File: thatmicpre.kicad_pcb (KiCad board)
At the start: 2 copper layers, 119.1 x 74.2 mm, 79 parts, among them J1 Barrel_Jack_Switch, J2 NC3FBH1, J3 NC3MBH2, Q1 BC546B, Q2 BC546B, SW1 SW_DPDT_x2, SW2 SW_DPDT_x2, SW3 SW_Rotary12, U1 THAT1510P08-U

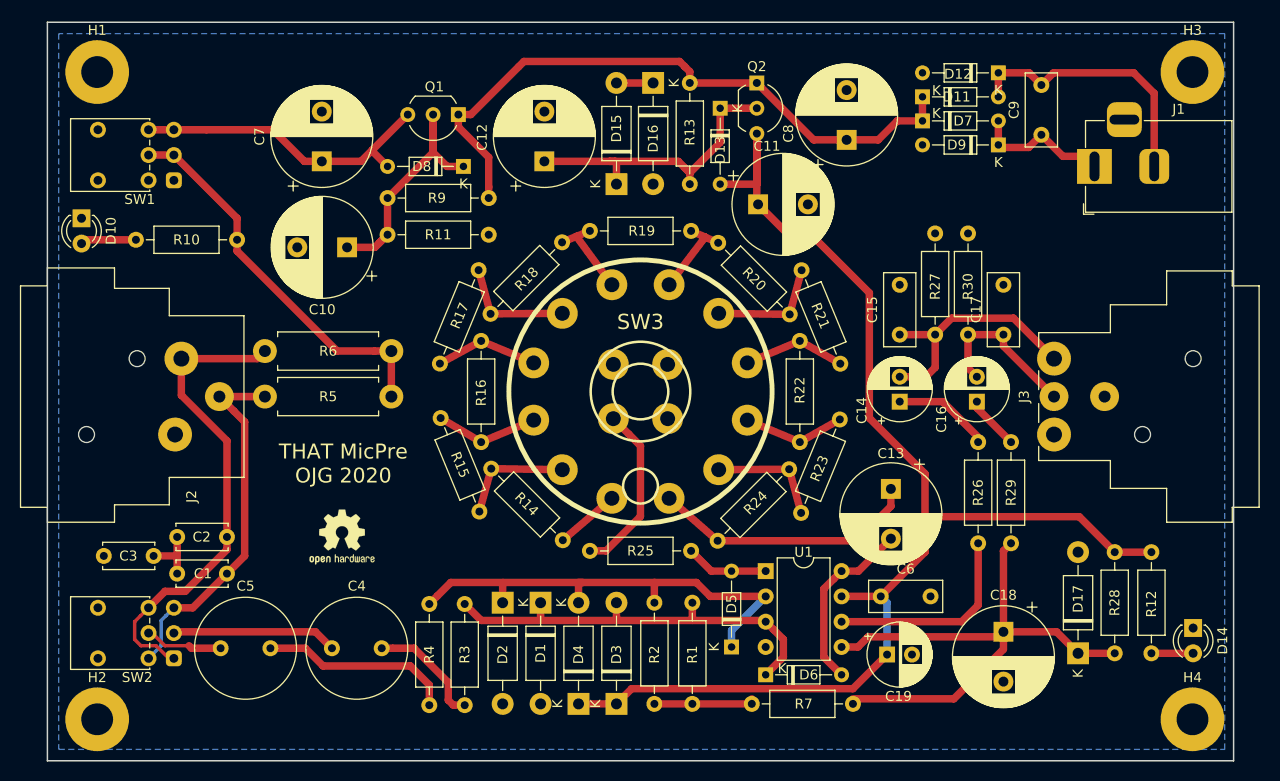
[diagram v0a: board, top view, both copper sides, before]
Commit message: Update to v1.1.
Add gerbers and pdfs to plots.
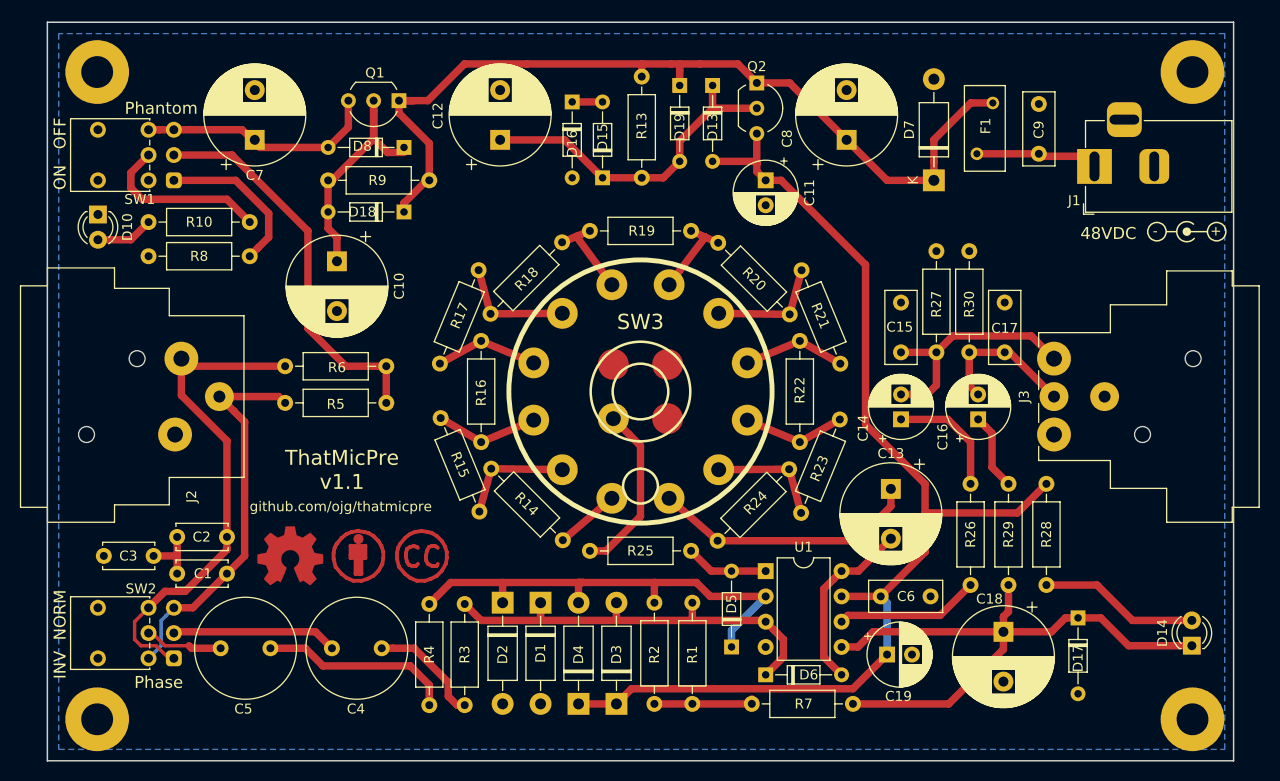
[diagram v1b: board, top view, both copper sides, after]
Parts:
- removed D11, D12, D9: 1N4148, Diode_THT:D_DO-34_SOD68_P7.62mm_Horizontal
- removed R11: 1Meg, Resistor_THT:R_Axial_DIN0207_L6.3mm_D2.5mm_P10.16mm_Horizontal
- removed R12: 27k, Resistor_THT:R_Axial_DIN0207_L6.3mm_D2.5mm_P10.16mm_Horizontal
- added D18: 1N4148, Diode_THT:D_DO-34_SOD68_P7.62mm_Horizontal, F.Cu at (86.6, 69.8)
- added D19: 1N4148, Diode_THT:D_DO-34_SOD68_P7.62mm_Horizontal, F.Cu at (114.3, 57.1)
- added F1: Polyfuse, Fuse:Fuse_BelFuse_0ZRE0005FF_L8.3mm_W3.8mm, F.Cu at (144.1, 64.0)
- added LOGO2: Logo_Open_Hardware_Small, Symbol:Symbol_CC-Attribution_CopperTop_Small, F.Cu at (82.0, 104.4)
- added LOGO3: Logo_Open_Hardware_Small, Symbol:Symbol_CreativeCommons_CopperTop_Type2_Small, F.Cu at (88.3, 104.5)
- added LOGO4: SYM_Arrow_Normal, Symbol:Symbol_Barrel_Polarity, F.Cu at (165.2, 71.8)
- added R8: 47k, Resistor_THT:R_Axial_DIN0207_L6.3mm_D2.5mm_P10.16mm_Horizontal, F.Cu at (71.1, 74.3)
- C11: value 220u-63V -> 47u-50V; footprint Capacitor_THT:CP_Radial_D10.0mm_P5.00mm -> Capacitor_THT:CP_Radial_D6.3mm_P2.50mm
- C13: value 2200u-6V3 -> 3300u-6V3
- C14, C16, C19: value 10u-63V -> 47u-50V
- C18: value 220u-63V -> 1000u-25V
- C4, C5: value 47u-63V -> 47u-63V-BP
- D15, D16, D17: value 15V -> 18V; footprint Diode_THT:D_DO-41_SOD81_P10.16mm_Horizontal -> Diode_THT:D_DO-34_SOD68_P7.62mm_Horizontal
- D7: value 1N4148 -> 1N4004; footprint Diode_THT:D_DO-34_SOD68_P7.62mm_Horizontal -> Diode_THT:D_DO-41_SOD81_P10.16mm_Horizontal
- J3: value NC3MBH2 -> NC3MBH1
- LOGO1: footprint Symbol:OSHW-Logo2_7.3x6mm_SilkScreen -> Symbol:OSHW-Symbol_6.7x6mm_Copper
- Q1, Q2: value BC546B -> BC546C
- R1, R2: value 1k2 -> 1k2-0.1%
- R10: value 39k -> 22k
- R13: value 47k -> 10k
- R14: value 100k -> 1M0
- R28: value 10k -> 4k7
- R3, R4: value 10R -> 10R-1W
- R5, R6: value 6k8-0.1%-1W -> 6k8-0.1%-0.5W; footprint Resistor_THT:R_Axial_DIN0411_L9.9mm_D3.6mm_P12.70mm_Horizontal -> Resistor_THT:R_Axial_DIN0207_L6.3mm_D2.5mm_P10.16mm_Horizontal
- moved R28 9.70 mm to (151.1, 97.2)
- moved D16 8.35 mm to (103.5, 58.8)
- moved C7 7.07 mm to (71.6, 62.6)
- moved D8 6.27 mm to (86.6, 63.4)
- moved R9 6.23 mm to (89.2, 66.7)
- moved Q1 6.13 mm to (86.1, 58.7)
- moved D7 6.08 mm to (139.8, 66.7), turned to 90 degrees
- moved LOGO1 5.54 mm to (75.2, 104.4)
- moved C12 4.94 mm to (96.3, 62.6)
- moved R13 4.87 mm to (110.5, 56.3)
- moved R26 4.26 mm to (143.5, 97.2)
- moved R29 4.20 mm to (147.3, 97.2)
- moved D17 3.56 mm to (154.3, 110.6), turned to 270 degrees
- moved C11 2.53 mm to (122.9, 66.7), turned to 270 degrees
- moved D13 2.41 mm to (117.6, 57.1)
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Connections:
- C9 pad 2: Net-(C9-Pad2) -> GND
- D14 pad 1: GND -> Net-(C18-Pad1)
- D7 pad 2: Net-(C9-Pad1) -> GND
- J1 pad 2: Net-(C9-Pad2) -> GND
- J3 pad G: GND -> (no net)
- R28 pad 2: Net-(C18-Pad1) -> Net-(D14-Pad2)
- R5 pad 1: Net-(R10-Pad1) -> Net-(R5-Pad1)
- R6 pad 1: Net-(R10-Pad1) -> Net-(R5-Pad1)
- SW1 pad 1: GND -> Net-(R8-Pad1)
- SW1 pad 2: Net-(R10-Pad1) -> Net-(R5-Pad1)
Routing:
- net Net-(R5-Pad1): track 0.00 -> 39.5 mm
- net Net-(C9-Pad2): track 26.3 -> 0.00 mm
- net Net-(C8-Pad1): track 65.6 -> 91.3 mm
- net Net-(R10-Pad1): track 39.0 -> 17.4 mm
- net Net-(R8-Pad1): track 0.00 -> 16.0 mm
- net Net-(D14-Pad2): track 4.19 -> 16.3 mm
- net Net-(C11-Pad1): track 132.1 -> 120.6 mm
- net Net-(C7-Pad1): track 31.6 -> 24.3 mm
- net Net-(R26-Pad2): track 20.6 -> 14.5 mm
- net Net-(C18-Pad1): track 57.1 -> 61.6 mm
- net Net-(C14-Pad1): track 9.53 -> 12.1 mm
- net Net-(C12-Pad1): track 31.2 -> 33.7 mm
- net Net-(C1-Pad1): track 37.0 -> 39.3 mm
- net Net-(C16-Pad1): track 5.48 -> 7.74 mm
- net Net-(C2-Pad1): track 48.5 -> 50.6 mm
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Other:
- board text added: "+"
- board text added: "-"
- board text added: "48VDC"
- board text added: "INV NORM"
- board text added: "ON OFF"
- board text added: "Phantom"
- board text added: "Phase"
- board text added: "ThatMicPre v1.1"
- board text added: "github.com/ojg/thatmicpre"
- board text removed: "THAT MicPre OJG 2020"

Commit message: Update project files to Kicad 6
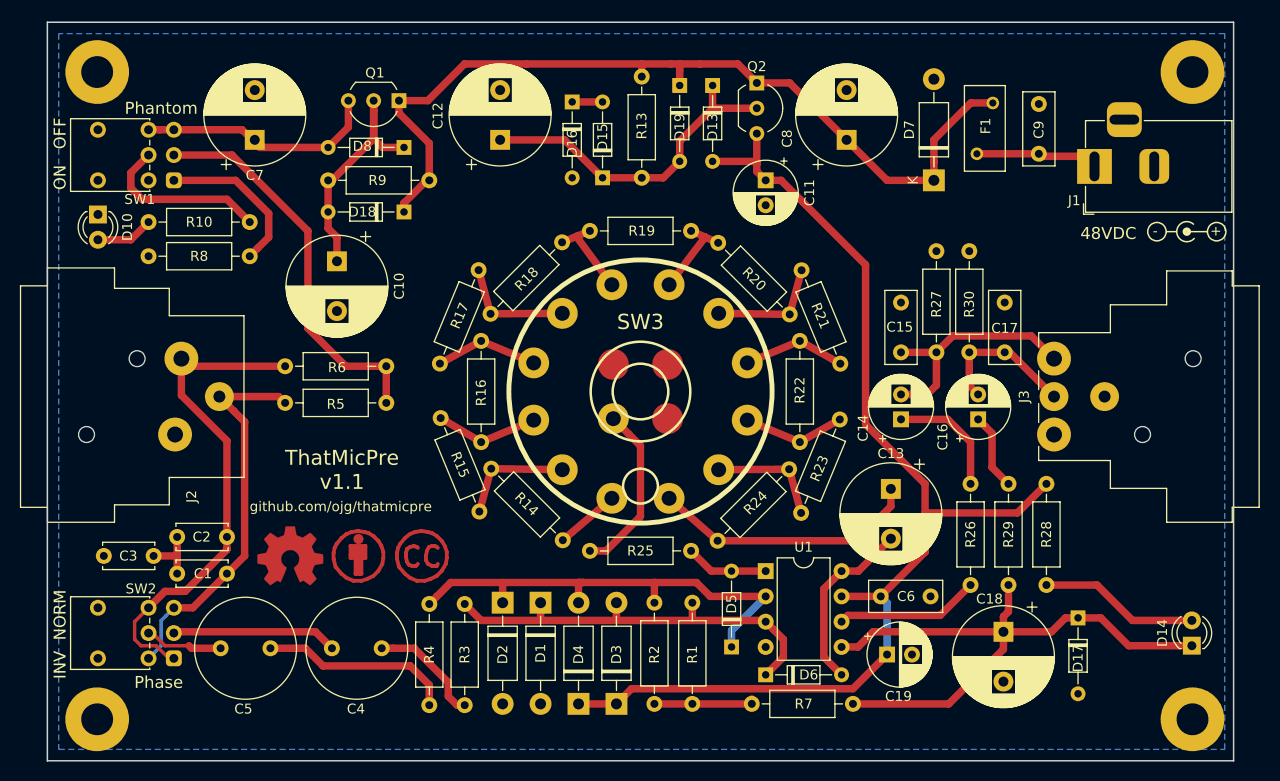
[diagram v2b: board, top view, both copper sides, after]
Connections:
- J1 pad 3: (no net) -> unconnected-(J1-Pad3)
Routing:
- net Net-(C8-Pad1): track 91.3 -> 89.8 mm
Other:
- net class Default removed
